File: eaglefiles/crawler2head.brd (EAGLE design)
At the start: 30 x 20 mm, 25 parts, among them U1 PCA9685

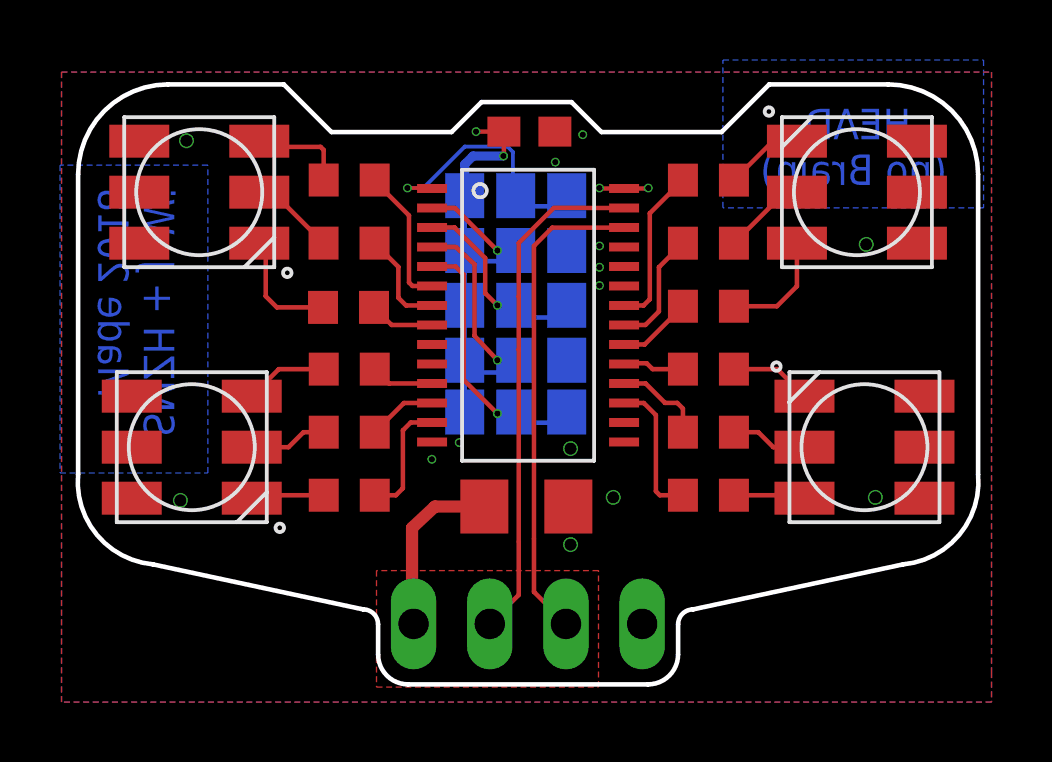
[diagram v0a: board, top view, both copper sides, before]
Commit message: fixed min distance
Signed-off-by: Julian Wingert <julian.wingert@subtilitas.de>
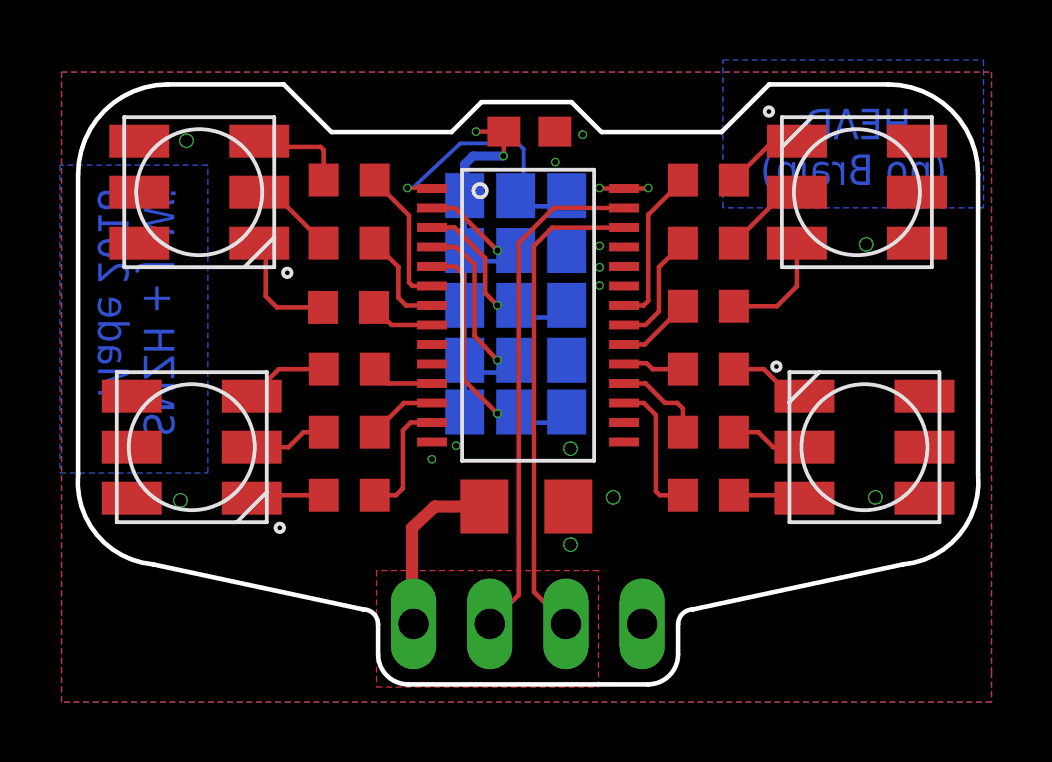
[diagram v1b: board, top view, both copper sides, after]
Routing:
- net N$5: track 6.48 -> 7.08 mm
